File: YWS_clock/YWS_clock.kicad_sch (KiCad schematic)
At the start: 62 parts, among them J1 Conn_01x06, J2 Power_inlet_vertical, J3 Conn_01x06, J4 Conn_02x03_Odd_Even, SW1 Omron_B3F_SPST, SW2 Omron_B3F_SPST, SW3 Omron_B3F_SPST, SW4 Omron_B3F_SPST, U1 L7805, U2 ATmega328-PU, U3 DS1307_DIP-8, U4 MAX7219, U5 MAX7219, U6 MAX7219, U7 MAX7219, Y1 Crystal_32768Hz, Y2 Crystal_16MHz

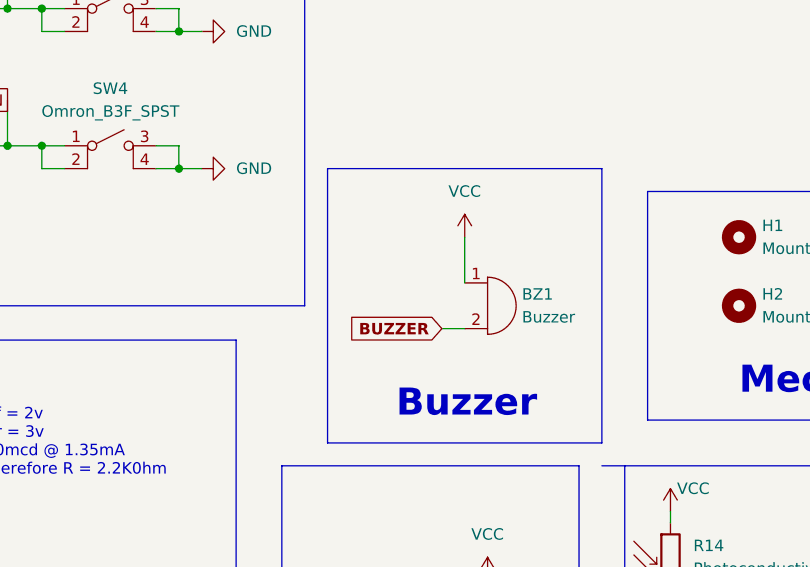
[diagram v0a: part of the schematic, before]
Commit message: update with modified PCB
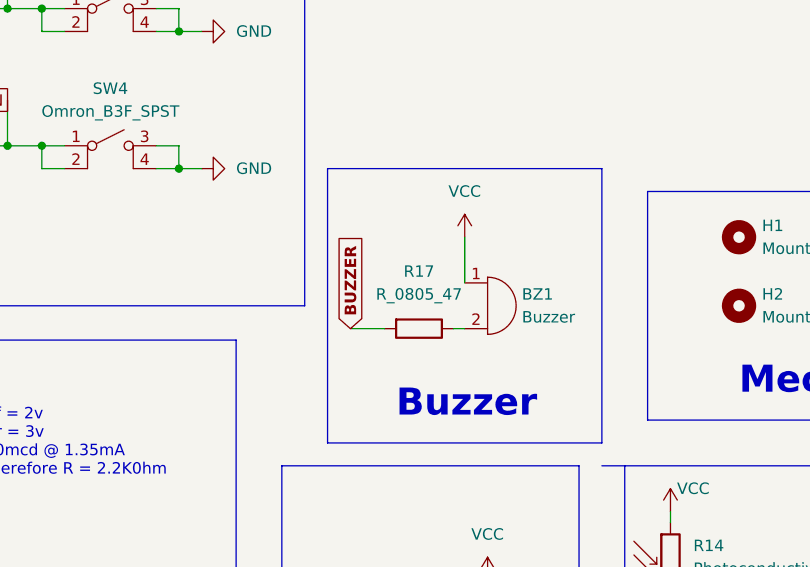
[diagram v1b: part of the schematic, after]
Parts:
- added R17: R_0805_47, footprints:R_0805_2012Metric, symbol HPS:R_0805_47
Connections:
- net BUZZER: now also R17.2; no longer BZ1.2 (+)
- new net: BZ1.2 (+), R17.1
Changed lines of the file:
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@@
     (stroke (width 0) (type default) (color 0 0 0 0))
   )
-  (wire (pts (xy 93.98 175.26) (xy 96.52 175.26))
-    (stroke (width 0) (type default) (color 0 0 0 0))
-  )
   (wire (pts (xy 119.38 36.83) (xy 119.38 48.26))
     (stroke (width 0) (type default) (color 0 0 0 0))
@@
     (stroke (width 0) (type default) (color 0 0 0 0))
   )
+  (wire (pts (xy 95.25 175.26) (xy 96.52 175.26))
+    (stroke (width 0) (type default) (color 0 0 0 0))
+  )
   (wire (pts (xy 231.14 45.72) (xy 246.38 45.72))
     (stroke (width 0) (type default) (color 0 0 0 0))
@@
     (stroke (width 0) (type default) (color 0 0 0 0))
   )
+  (wire (pts (xy 83.82 175.26) (xy 87.63 175.26))
+    (stroke (width 0) (type default) (color 0 0 0 0))
+  )
   (polyline (pts (xy 81.28 157.48) (xy 111.76 157.48))
     (stroke (width 0) (type default) (color 0 0 0 0))
@@
     )
   )
-  (global_label "BUZZER" (shape input) (at 93.98 175.26 180) (fields_autoplaced)
-    (effects (font (size 1.27 1.27) bold) (justify right))
-    (property "Intersheet References" "${INTERSHEET_REFS}" (id 0) (at 83.9379 175.387 0)
+  (global_label "BUZZER" (shape input) (at 83.82 175.26 90) (fields_autoplaced)
+    (effects (font (size 1.27 1.27) bold) (justify left))
+    (property "Intersheet References" "${INTERSHEET_REFS}" (id 0) (at 83.693 165.2179 90)
       (effects (font (size 1.27 1.27) bold) (justify left) hide)
     )
@@
     (pin "8")
   )
+  (symbol (lib_id "HPS:R_0805_47") (at 91.44 175.26 270) (unit 1)
+    (in_bom yes) (on_board yes) (fields_autoplaced)
+    (property "Reference" "R17" (id 0) (at 91.44 168.91 90))
+    (property "Value" "R_0805_47" (id 1) (at 91.44 171.45 90))
+    (property "Footprint" "footprints:R_0805_2012Metric" (id 2) (at 74.93 175.26 0)
+      (effects (font (size 1.27 1.27)) hide)
+    )
+    (property "Datasheet" "https://www.digikey.com/en/products/detail/yageo/RC0805FR-0747RL/727972" (id 3) (at 91.44 172.72 0)
+      (effects (font (size 1.27 1.27)) hide)
+    )
+    (property "MFG" "Yageo" (id 4) (at 80.01 175.26 0)
+      (effects (font (size 1.27 1.27)) hide)
+    )
+    (property "Digikey PN" "RC0805FR-0747RL " (id 5) (at 77.47 175.26 0)
+      (effects (font (size 1.27 1.27)) hide)
+    )
+    (property "Mouser PN" "N/A" (id 6) (at 64.77 175.26 0)
+      (effects (font (size 1.27 1.27)) hide)
+    )
+    (property "Power" "N/A" (id 7) (at 67.31 175.26 0)
+      (effects (font (size 1.27 1.27)) hide)
+    )
+    (property "Tolerance" "N/A" (id 8) (at 69.85 175.26 0)
+      (effects (font (size 1.27 1.27)) hide)
+    )
+    (property "MPN" "RC0805FR-0747RL " (id 9) (at 72.39 175.26 0)
+      (effects (font (size 1.27 1.27)) hide)
+    )
+    (pin "1")
+    (pin "2")
+  )
   (symbol (lib_id "HPS:R_0805_10K") (at 160.02 104.14 0) (unit 1)
     (in_bom yes) (on_board yes)
@@
       (reference "R16") (unit 1) (value "R_0805_2.2K") (footprint "footprints:R_0805_2012Metric")
     )
+    (path "/752465b5-60ba-4ddc-9fc5-5a14209341c2"
+      (reference "R17") (unit 1) (value "R_0805_47") (footprint "footprints:R_0805_2012Metric")
+    )
     (path "/1e455009-0c28-46b0-8494-f63ccf6d3227"

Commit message: 3 error fixed
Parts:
- removed C1: C_0805_10uf, footprints:C_0805_2012Metric, symbol HPS:C_0805_10uf
- removed D6: LED_0805, footprints:LED_0805_2012Metric, symbol HPS:LED_0805
- removed J2: Power_inlet_vertical, footprints:Wurth-694106402002, symbol HPS:Power_inlet_vertical
- removed R16: R_0805_2.2K, footprints:R_0805_2012Metric, symbol HPS:R_0805_2.2K
- added C1: C_0805_0.1uf, footprints:C_0805_2012Metric, symbol HPS:C_0805_0.1uf
- added J2: PJ-102AH, footprints:PJ-102AH, symbol HPS:PJ-102AH
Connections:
- net GND: now also C1.2, J2.2 (OUT)
- net at C6.1, U1.1 (IN): now also J2.1 (POLE)
- net at U2.21 (AREF): now also C1.1
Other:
- note removed: "IO_LED"
